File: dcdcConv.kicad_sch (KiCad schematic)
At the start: 82 parts, among them J11 Conn_01x03, J12 EN, J13 Conn_01x03, J21 PWRSWITCH, J22 Conn_01x02, J23 PGOOD, U11 TLV62130, U21 UM1550S-18, U6 TLV62130, U8 TLV62130, U9 MAX42402AFLB+

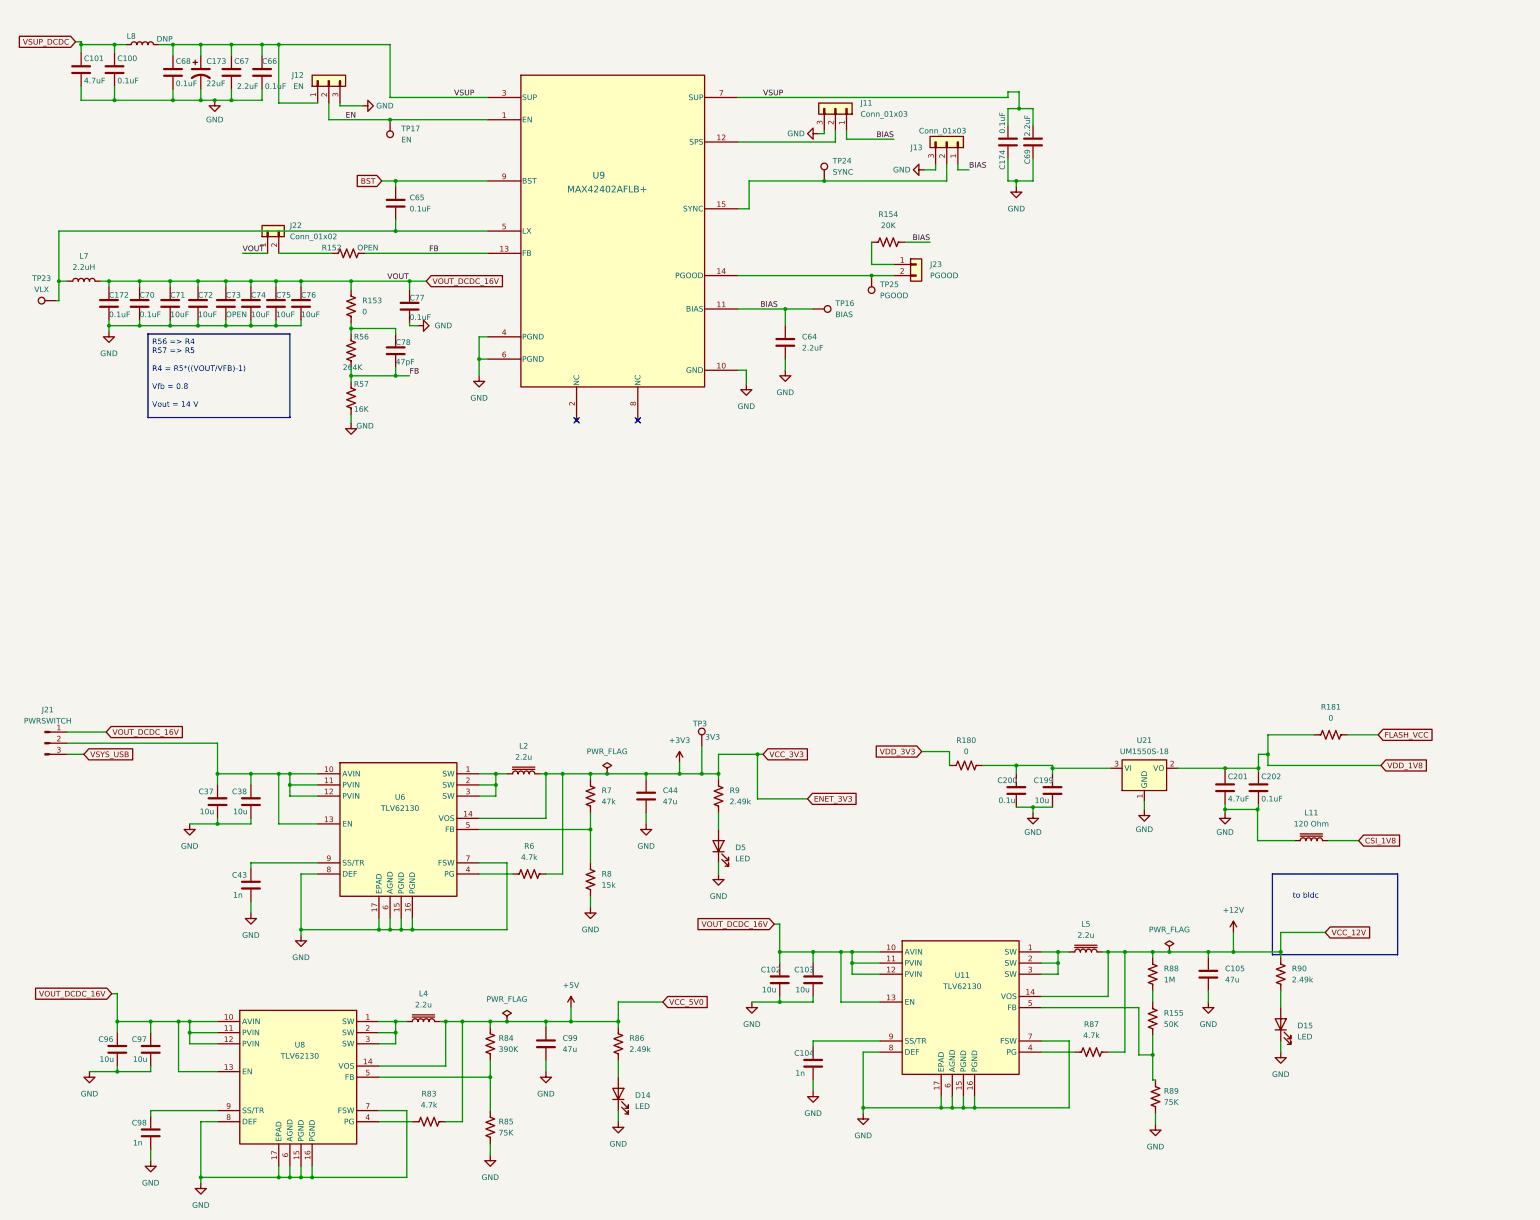
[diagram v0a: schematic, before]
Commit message: add revision to motor
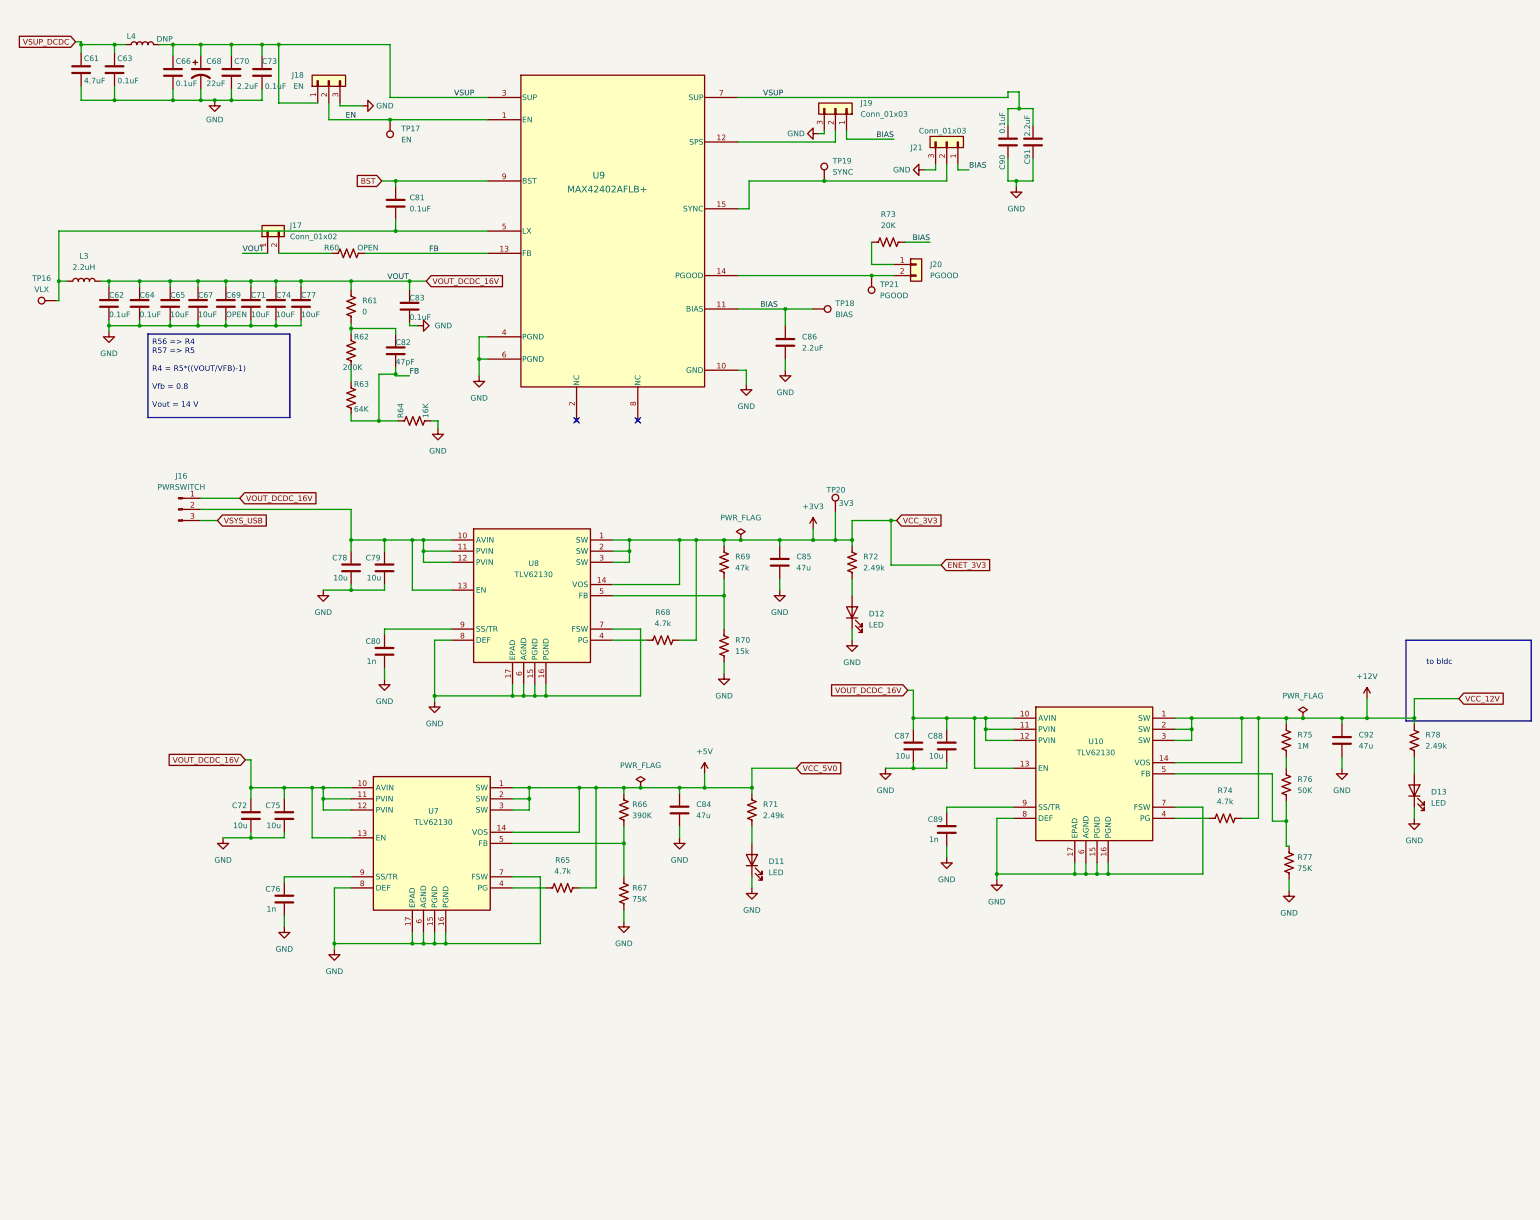
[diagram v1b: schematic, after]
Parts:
- removed C199: 10u, Capacitor_SMD:C_0603_1608Metric, symbol Device:C
- removed C200: 0.1u, Capacitor_SMD:C_0402_1005Metric, symbol Device:C
- removed C201: 4.7uF, Capacitor_SMD:C_0402_1005Metric, symbol Device:C
- removed C202: 0.1uF, Capacitor_SMD:C_0402_1005Metric, symbol Device:C
- removed L11: 120 Ohm, Inductor_SMD:L_APV_APH0620, symbol Device:L_Iron
- removed L2, L4, L5: 2.2u, Inductor_SMD:L_APV_APH0620, symbol Device:L_Iron
- removed R180, R181: 0, Resistor_SMD:R_0402_1005Metric, symbol Device:R_US
- removed U21: UM1550S-18, Package_TO_SOT_SMD:SOT-223-3_TabPin2, symbol Regulator_Linear:AMS1117-1.8
- added R64: 16K, Resistor_SMD:R_0402_1005Metric, symbol Device:R_US
- R62: renamed from R56; value 264K -> 200K; footprint Resistor_SMD:R_0402_1005Metric -> Resistor_SMD:R_0603_1608Metric
- R63: renamed from R57; value 16K -> 64K; footprint Resistor_SMD:R_0402_1005Metric -> Resistor_SMD:R_0603_1608Metric
- renumbered C101 to C61, C172 to C62, C100 to C63, C70 to C64, C71 to C65, C68 to C66, C72 to C67, C173 to C68, C73 to C69, C67 to C70, C74 to C71, C96 to C72, C66 to C73, C75 to C74, C97 to C75, C98 to C76, C76 to C77, C37 to C78, C38 to C79, C43 to C80, C65 to C81, C78 to C82, C77 to C83, C99 to C84, C44 to C85, C64 to C86, C102 to C87, C103 to C88, C104 to C89, C174 to C90, C69 to C91, C105 to C92, D14 to D11, D5 to D12, D15 to D13, J21 to J16, J22 to J17, J12 to J18, J11 to J19, J23 to J20, J13 to J21, L7 to L3, L8 to L4, R152 to R60, R153 to R61, R83 to R65, R84 to R66, R85 to R67, R6 to R68, R7 to R69, R8 to R70, R86 to R71, R9 to R72, R154 to R73, R87 to R74, R88 to R75, R155 to R76, R89 to R77, R90 to R78, TP23 to TP16, TP16 to TP18, TP24 to TP19, TP3 to TP20, TP25 to TP21, U11 to U10, U8 to U7, U6 to U8
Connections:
- net +12V: now also U10.1 (SW), U10.2 (SW), U10.3 (SW)
- net +3V3: now also U8.1 (SW), U8.2 (SW), U8.3 (SW)
- net +5V: now also U7.1 (SW), U7.2 (SW), U7.3 (SW)
- net FB: now also R63.2, R64.1; no longer R62.2, R63.1
- net GND: now also R64.2; no longer R63.2
- new net: R62.2, R63.1
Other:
- moved on the sheet: C72, C75, C76, C78, C79, C80, C84, C85, C87, C88, C89, C92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

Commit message: del some
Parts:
- renumbered J16 to J17, J17 to J18, J18 to J19, J19 to J20, J20 to J21, J21 to J22
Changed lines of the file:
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@@
 		(on_board yes)
 		(dnp no)
-		(property "Reference" "J21"
+		(property "Reference" "J22"
 			(at 217.805 38.735 90)
 			(effects
@@
 			(project "qiot"
 				(path "/0db193be-516d-4409-bb62-b8733a9e8874/65f7929d-7798-4764-abd1-5709ade91827"
-					(reference "J21")
+					(reference "J22")
 					(unit 1)
 				)
@@
 		(dnp no)
 		(fields_autoplaced yes)
-		(property "Reference" "J17"
+		(property "Reference" "J18"
 			(at 76.2 56.5149 90)
 			(effects
@@
 			(project ""
 				(path "/0db193be-516d-4409-bb62-b8733a9e8874/65f7929d-7798-4764-abd1-5709ade91827"
-					(reference "J17")
+					(reference "J18")
 					(unit 1)
 				)
@@
 		(on_board yes)
 		(dnp no)
-		(property "Reference" "J18"
+		(property "Reference" "J19"
 			(at 79.375 22.2249 90)
 			(effects
@@
 			(project "qiot"
 				(path "/0db193be-516d-4409-bb62-b8733a9e8874/65f7929d-7798-4764-abd1-5709ade91827"
-					(reference "J18")
+					(reference "J19")
 					(unit 1)
 				)
@@
 		(dnp no)
 		(fields_autoplaced yes)
-		(property "Reference" "J20"
+		(property "Reference" "J21"
 			(at 222.25 65.4049 0)
 			(effects
@@
 			(project ""
 				(path "/0db193be-516d-4409-bb62-b8733a9e8874/65f7929d-7798-4764-abd1-5709ade91827"
-					(reference "J20")
+					(reference "J21")
 					(unit 1)
 				)
@@
 		(dnp no)
 		(fields_autoplaced yes)
-		(property "Reference" "J19"
+		(property "Reference" "J20"
 			(at 206.375 28.5749 90)
 			(effects
@@
 			(project ""
 				(path "/0db193be-516d-4409-bb62-b8733a9e8874/65f7929d-7798-4764-abd1-5709ade91827"
-					(reference "J19")
+					(reference "J20")
 					(unit 1)
 				)
@@
 		(dnp no)
 		(fields_autoplaced yes)
-		(property "Reference" "J16"
+		(property "Reference" "J17"
 			(at 51.435 113.665 0)
 			(effects
@@
 			(project ""
 				(path "/0db193be-516d-4409-bb62-b8733a9e8874/65f7929d-7798-4764-abd1-5709ade91827"
-					(reference "J16")
+					(reference "J17")
 					(unit 1)
 				)

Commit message: dad
da
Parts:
- C61: Manufacturer_Part_Number (none) -> CL05A475MP5NRNC
- C62, C63, C64, C66, C73, C81, C83, C90: value 0.1uF -> 100nF; Manufacturer_Part_Number (none) -> CS1005X7R104K500NR
- C65, C67, C71, C74, C77: Manufacturer_Part_Number (none) -> CS1608X5R106M160NRB
- C68: Manufacturer_Part_Number (none) -> CL10A226MQ8NRNC
- C69, J17, J18, J19, J20, J21, J22, L4, R60, TP16, TP17, TP18, TP19, TP20, TP21: now not fitted
- C70, C86, C91: Manufacturer_Part_Number (none) -> CL05A225MQ5NSNC
- C72, C75, C78, C79, C87, C88: value 10u -> 10uF; Manufacturer_Part_Number (none) -> CS1608X5R106M160NRB
- C76, C80, C89: value 1n -> 1nF; Manufacturer_Part_Number (none) -> TCC0402X7R102M500AT
- C82: Manufacturer_Part_Number (none) -> CC0402JRNPO9BN470
- C84, C85, C92: value 47u -> 47uF; Manufacturer_Part_Number (none) -> 0603X476M6R3NT
- D11, D12, D13: Manufacturer_Part_Number (none) -> C6210741
- L3: Manufacturer_Part_Number (none) -> AFE201612S2R2MBT
- R61: Manufacturer_Part_Number (none) -> RC0402FR-070RL
- R62: Manufacturer_Part_Number (none) -> FRC0603F2003TS
- R63: Manufacturer_Part_Number (none) -> ARG03DTC6402N
- R64: Manufacturer_Part_Number (none) -> RC0402FR-0716KL
- R65, R68, R74: value 4.7k -> 4.7K; Manufacturer_Part_Number (none) -> RC0402FR-074K7L
- R66: Manufacturer_Part_Number (none) -> 0402WGF3903TCE
- R67, R77: Manufacturer_Part_Number (none) -> RC0402FR-0775KL
- R69: value 47k -> 47K; Manufacturer_Part_Number (none) -> RC0402FR-0747KL
- R70: value 15k -> 15K; Manufacturer_Part_Number (none) -> 0402WGF1502TCE
- R71, R72, R78: value 2.49k -> 2.49K; Manufacturer_Part_Number (none) -> RTT022491FTH
- R73: Manufacturer_Part_Number (none) -> 0402WGF2002TCE
- R75: Manufacturer_Part_Number (none) -> RC0402FR-071ML
- R76: Manufacturer_Part_Number (none) -> RTT025002FTH
- U10, U7, U8: Manufacturer_Part_Number (none) -> TLV62130RGTR
- U9: Manufacturer_Part_Number (none) -> MAX42402AFLB+

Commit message: gema
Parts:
- added L5, L6, L7: L, symbol Device:L
- added R19, R23: 10K, Resistor_SMD:R_0402_1005Metric, symbol Device:R_US
- C61:  LCSC Part # (none) -> C2858031; Manufacturer_Part_Number CL05A475MP5NRNC -> GRM155R61E475ME15D
- C62, C63, C64, C66, C73, C81, C83, C90:  LCSC Part # (none) -> C77020; Manufacturer_Part_Number CS1005X7R104K500NR -> GRM155R71H104KE14D
- C65, C67, C71, C72, C74, C75, C77, C78, C79, C87, C88:  LCSC Part # (none) -> C194427; Manufacturer_Part_Number CS1608X5R106M160NRB -> GRM188R6YA106MA73D
- C68: footprint Capacitor_SMD:C_0603_1608Metric -> footprints:CAP-SMD_L7.3-W4.3-R-RD;  LCSC Part # (none) -> C696800; Manufacturer_Part_Number CL10A226MQ8NRNC -> T491X226K050AT
- C70, C86, C91:  LCSC Part # (none) -> C385032; Manufacturer_Part_Number CL05A225MQ5NSNC -> GRM155R61E225KE11D
- C76, C80, C89:  LCSC Part # (none) -> C696907
- C82:  LCSC Part # (none) -> C105622; Manufacturer_Part_Number CC0402JRNPO9BN470 -> CC0603JRNPO9BN470
- C84, C85:  LCSC Part # (none) -> C140782; Manufacturer_Part_Number 0603X476M6R3NT -> GRM188R60J476ME15D
- C92: footprint Capacitor_SMD:C_0603_1608Metric -> Capacitor_SMD:C_1206_3216Metric;  LCSC Part # (none) -> C403725; Manufacturer_Part_Number 0603X476M6R3NT -> GRM31CR61E476ME44L
- D11, D12, D13:  LCSC Part # (none) -> C6210741
- L3:  LCSC Part # (none) -> C41347750
- R61:  LCSC Part # (none) -> C106231
- R62:  LCSC Part # (none) -> C2907009
- R63:  LCSC Part # (none) -> C2902643
- R64:  LCSC Part # (none) -> C163487
- R65, R68, R74:  LCSC Part # (none) -> C105871
- R66:  LCSC Part # (none) -> C25782
- R67, R77:  LCSC Part # (none) -> C137935
- R69:  LCSC Part # (none) -> C93943
- R70:  LCSC Part # (none) -> C25756
- R71, R72, R78:  LCSC Part # (none) -> C102924
- R73:  LCSC Part # (none) -> C25765
- R75:  LCSC Part # (none) -> C138033
- R76: footprint Resistor_SMD:R_0402_1005Metric -> Resistor_SMD:R_0603_1608Metric;  LCSC Part # (none) -> C861451; Manufacturer_Part_Number RTT025002FTH -> RT0603BRD0750KL
- U10, U7, U8:  LCSC Part # (none) -> C122479
- U9:  LCSC Part # (none) -> C22392296
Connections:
- net +12V: now also L7.2; no longer U10.1 (SW), U10.2 (SW), U10.3 (SW)
- net +3V3: now also L6.2; no longer U8.1 (SW), U8.2 (SW), U8.3 (SW)
- net +5V: now also L5.2; no longer U7.1 (SW), U7.2 (SW), U7.3 (SW)
- net GND: now also R19.2, R23.2
- net VOUT_DCDC_16V: now also R19.1, R23.1
- new net: L7.1, U10.1 (SW), U10.2 (SW), U10.3 (SW)
- new net: L5.1, U7.1 (SW), U7.2 (SW), U7.3 (SW)
- new net: L6.1, U8.1 (SW), U8.2 (SW), U8.3 (SW)
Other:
- moved on the sheet: C66
